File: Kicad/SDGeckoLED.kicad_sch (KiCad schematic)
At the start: 8 parts, among them J4 MICRO-SD-CARD, U1 74AHC1G32

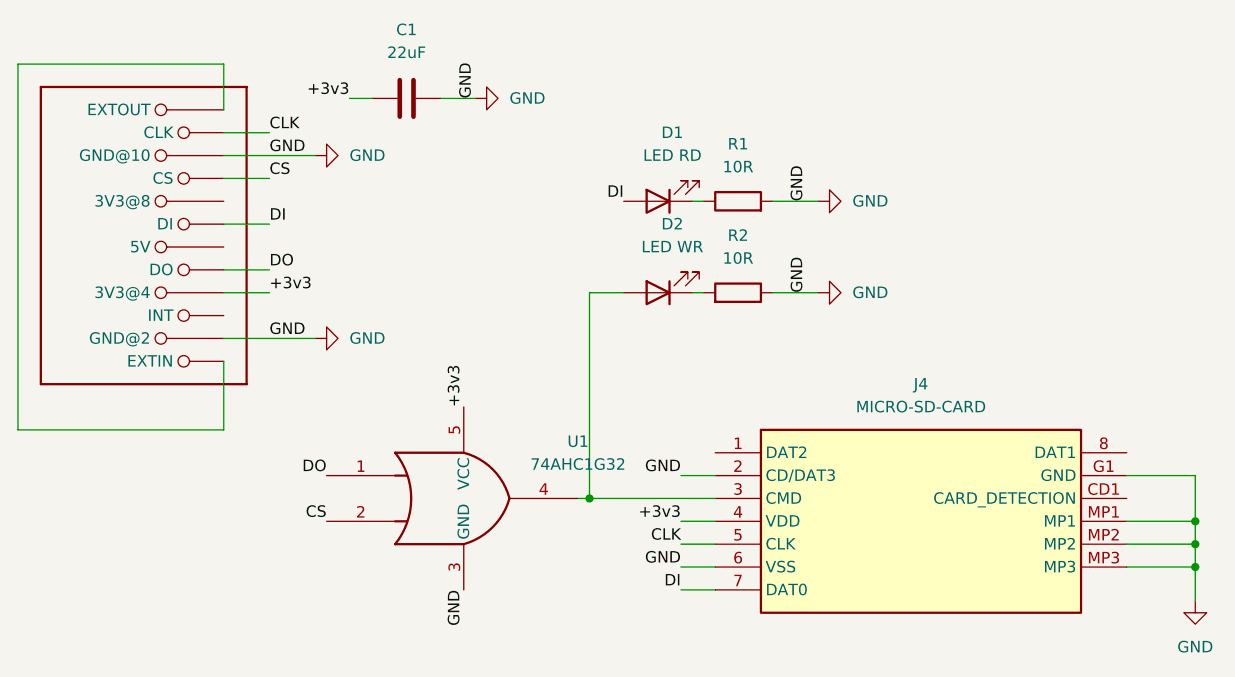
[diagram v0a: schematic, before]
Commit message: updated kicad project for sd gerber fix
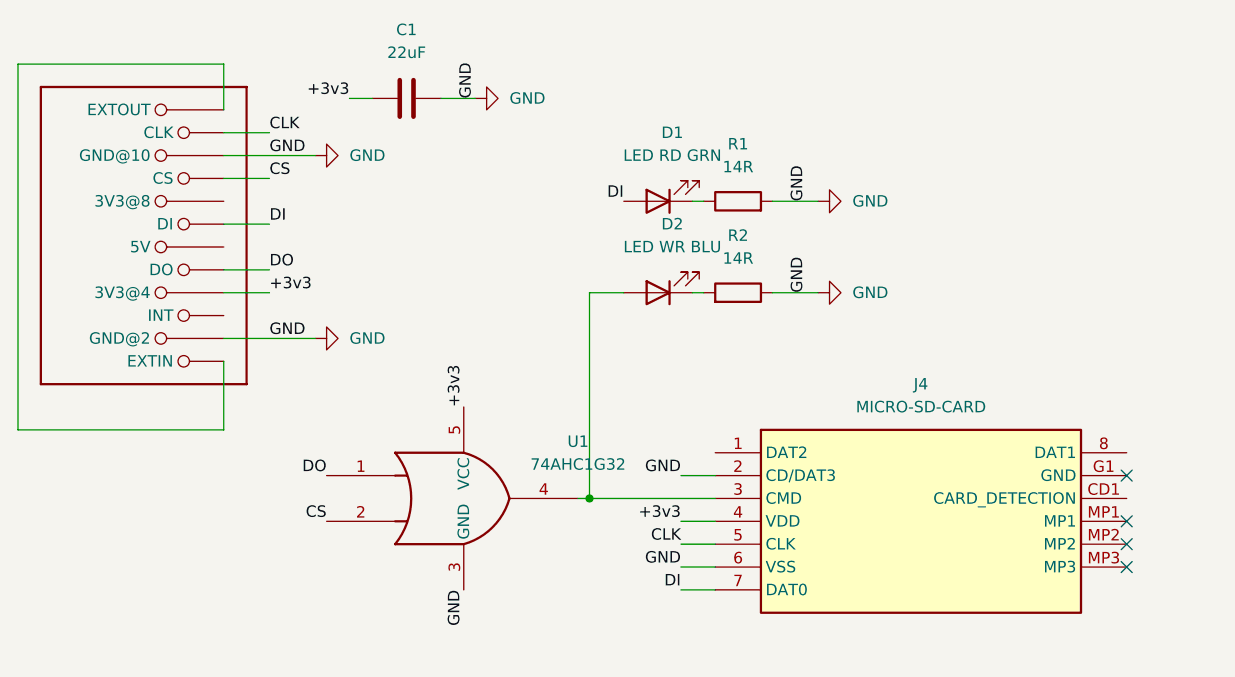
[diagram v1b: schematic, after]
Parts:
- C1: LCSC PN (none) -> C3845593
- D1: value LED RD -> LED RD GRN; LCSC PN (none) -> C2856703
- D2: value LED WR -> LED WR BLU; LCSC PN (none) -> C965797
- J2: now left out of the parts list
- J4: LCSC PN (none) -> C113206
- R1, R2: value 10R -> 14R; LCSC PN (none) -> C400609
- U1: LCSC PN (none) -> C12488
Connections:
- net GND: no longer J4.G1 (GND), J4.MP1, J4.MP2, J4.MP3
- no-connect marks 0 -> 4
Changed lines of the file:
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@@
 	(paper "A4")
-	(junction
-		(at 226.06 115.57)
-		(diameter 0)
-		(color 0 0 0 0)
-	)
 	(junction
 		(at 158.75 113.03)
@@
 		(color 0 0 0 0)
 	)
-	(junction
-		(at 226.06 118.11)
-		(diameter 0)
-		(color 0 0 0 0)
-	)
-	(junction
-		(at 226.06 120.65)
-		(diameter 0)
-		(color 0 0 0 0)
-	)
-	(wire
-		(pts
-			(xy 226.06 120.65) (xy 226.06 124.46)
-		)
-		(stroke
-			(width 0)
-			(type default)
-		)
+	(no_connect
+		(at 218.44 110.49)
+	)
+	(no_connect
+		(at 218.44 115.57)
+	)
+	(no_connect
+		(at 218.44 120.65)
+	)
+	(no_connect
+		(at 218.44 118.11)
 	)
 	(wire
@@
 	(wire
 		(pts
-			(xy 226.06 110.49) (xy 226.06 115.57)
-		)
-		(stroke
-			(width 0)
-			(type default)
-		)
-	)
-	(wire
-		(pts
-			(xy 226.06 118.11) (xy 226.06 120.65)
-		)
-		(stroke
-			(width 0)
-			(type default)
-		)
-	)
-	(wire
-		(pts
 			(xy 118.11 105.41) (xy 118.11 97.79)
 		)
@@
 	(wire
 		(pts
-			(xy 218.44 115.57) (xy 226.06 115.57)
-		)
-		(stroke
-			(width 0)
-			(type default)
-		)
-	)
-	(wire
-		(pts
 			(xy 179.07 90.17) (xy 184.15 90.17)
 		)
@@
 	(wire
 		(pts
-			(xy 226.06 115.57) (xy 226.06 118.11)
-		)
-		(stroke
-			(width 0)
-			(type default)
-		)
-	)
-	(wire
-		(pts
 			(xy 158.75 90.17) (xy 158.75 113.03)
 		)
@@
 	(wire
 		(pts
-			(xy 218.44 118.11) (xy 226.06 118.11)
-		)
-		(stroke
-			(width 0)
-			(type default)
-		)
-	)
-	(wire
-		(pts
-			(xy 218.44 120.65) (xy 226.06 120.65)
-		)
-		(stroke
-			(width 0)
-			(type default)
-		)
-	)
-	(wire
-		(pts
 			(xy 179.07 80.01) (xy 184.15 80.01)
 		)
@@
 		(pts
 			(xy 123.19 87.63) (xy 118.11 87.63)
-		)
-		(stroke
-			(width 0)
-			(type default)
-		)
-	)
-	(wire
-		(pts
-			(xy 218.44 110.49) (xy 226.06 110.49)
 		)
 		(stroke
@@
 			)
 		)
+		(property "LCSC PN" "C3845593"
+			(at 138.43 68.58 90)
+			(effects
+				(font
+					(size 1.27 1.27)
+				)
+				(hide yes)
+			)
+		)
 		(pin "1"
 		)
@@
 			)
 		)
-		(property "Value" "LED WR"
+		(property "Value" "LED WR BLU"
 			(at 167.9575 85.09 0)
 			(effects
@@
 		)
 		(property "Description" ""
+			(at 166.37 90.17 0)
+			(effects
+				(font
+					(size 1.27 1.27)
+				)
+				(hide yes)
+			)
+		)
+		(property "LCSC PN" "C965797"
 			(at 166.37 90.17 0)
 			(effects
@@
 				(path "/7df071e1-7397-44f5-b59a-b874d632f1c4"
 					(reference "D2")
-					(unit 1)
-				)
-			)
-		)
-	)
-	(symbol
-		(lib_id "power:GND")
-		(at 226.06 124.46 0)
-		(unit 1)
-		(exclude_from_sim no)
-		(in_bom yes)
-		(on_board yes)
-		(dnp no)
-		(fields_autoplaced yes)
-		(property "Reference" "#PWR02"
-			(at 226.06 130.81 0)
-			(effects
-				(font
-					(size 1.27 1.27)
-				)
-				(hide yes)
-			)
-		)
-		(property "Value" "GND"
-			(at 226.06 129.54 0)
-			(effects
-				(font
-					(size 1.27 1.27)
-				)
-			)
-		)
-		(property "Footprint" ""
-			(at 226.06 124.46 0)
-			(effects
-				(font
-					(size 1.27 1.27)
-				)
-				(hide yes)
-			)
-		)
-		(property "Datasheet" ""
-			(at 226.06 124.46 0)
-			(effects
-				(font
-					(size 1.27 1.27)
-				)
-				(hide yes)
-			)
-		)
-		(property "Description" ""
-			(at 226.06 124.46 0)
-			(effects
-				(font
-					(size 1.27 1.27)
-				)
-				(hide yes)
-			)
-		)
-		(pin "1"
-		)
-		(instances
-			(project "SDGeckoLED"
-				(path "/7df071e1-7397-44f5-b59a-b874d632f1c4"
-					(reference "#PWR02")
 					(unit 1)
 				)
@@
 			)
 		)
+		(property "LCSC PN" "C113206"
+			(at 172.72 107.95 0)
+			(effects
+				(font
+					(size 1.27 1.27)
+				)
+				(hide yes)
+			)
+		)
 		(pin "1"
 		)
@@
 			)
 		)
+		(property "LCSC PN" "C12488"
+			(at 144.78 113.03 0)
+			(effects
+				(font
+					(size 1.27 1.27)
+				)
+				(hide yes)
+			)
+		)
 		(pin "5"
 		)
@@
 			)
 		)
-		(property "Value" "LED RD"
+		(property "Value" "LED RD GRN"
 			(at 167.9575 74.93 0)
 			(effects
@@
 		)
 		(property "Description" ""
+			(at 166.37 80.01 0)
+			(effects
+				(font
+					(size 1.27 1.27)
+				)
+				(hide yes)
+			)
+		)
+		(property "LCSC PN" "C2856703"
 			(at 166.37 80.01 0)
 			(effects
@@
 		(unit 1)
 		(exclude_from_sim no)
-		(in_bom yes)
+		(in_bom no)
 		(on_board yes)
 		(dnp no)
@@
 			)
 		)
-		(property "Value" "10R"
+		(property "Value" "14R"
 			(at 175.26 76.2 90)
 			(effects
@@
 		(property "Description" ""
 			(at 175.26 80.01 0)
+			(effects
+				(font
+					(size 1.27 1.27)
+				)
+				(hide yes)
+			)
+		)
+		(property "LCSC PN" "C400609"
+			(at 175.26 80.01 90)
 			(effects
 				(font
@@
 			)
 		)
-		(property "Value" "10R"
+		(property "Value" "14R"
 			(at 175.26 86.36 90)
 			(effects
@@
 			(effects
 				(font
+					(size 1.27 1.27)
+				)
+				(hide yes)
+			)
+		)
+		(property "LCSC PN" "C400609"
+			(at 175.26 90.17 90)
+			(effects
+				(font
